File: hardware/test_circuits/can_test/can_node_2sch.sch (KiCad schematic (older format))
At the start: 32 parts, among them J201 Conn_01x05_Female, SW201 CAN1_RST, SW202 SW_SPDT, U201 MCP2562-E-P, U202 MCP2515-xSO, U203 PIC18F4620-IP, U204 L7805, Y201 40MHz, Y202 10MHz

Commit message: Realized I probably want to actually use the ~INT pin on the MCP2515 for recognizing when a transmission has successfull occured... And if I'm using that, might as well also use it for RX interrupts as well...
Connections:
- net CAN2_~INT: now reaches U202.12 (~INT)
- net CAN2_~INT: now also U203.35 (RB2/INT2/AN8)
- net CAN2_~RESET: no longer names the net of R204.2, SW201.1, U202.17 (~RESET)
- net CAN2_~RESET: no longer U203.35 (RB2/INT2/AN8)
- no-connect marks 22 -> 21
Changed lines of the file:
@@
 	1    0    0    -1
 $EndComp
-NoConn ~ 8850 2550
 Text GLabel 7650 1950 0    50   Input ~ 0
 PIC2_MOSI
@@
 Wire Wire Line
 	9300 4050 9300 4000
-Text GLabel 9500 3550 2    30   Input ~ 0
-CAN2_~RESET
-Wire Wire Line
-	9300 3550 9500 3550
+Text GLabel 8850 2550 2    30   Input ~ 0
+CAN2_~INT
 $Comp
 L power:GND #PWR0204
@@
 Connection ~ 9300 2850
 Text GLabel 4800 2300 2    30   Input ~ 0
-CAN2_~RESET
+CAN2_~INT
 Text GLabel 4800 2600 2    30   Input ~ 0
 CAN2_~RX0BF
@@
 Wire Wire Line
 	5600 1850 5600 1950
+Text GLabel 4800 4400 2    50   Input ~ 0
+PIC2_~SS
 Wire Bus Line
 	1700 3750 1700 4850
@@
 Wire Bus Line
 	5000 3150 5000 3800
-Text GLabel 4800 4400 2    50   Input ~ 0
-PIC2_~SS
 $EndSCHEMATC

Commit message: ..
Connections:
- net +5VL: now also U202.10 (~RX1BF), U202.11 (~RX0BF)
- net CAN2_~INT: now also U203.33 (RB0/INT0/FLT0/AN12); no longer U203.35 (RB2/INT2/AN8)
- removed net CAN2_~RX0BF: U202.11 (~RX0BF), U203.33 (RB0/INT0/FLT0/AN12)
- net CAN2_~RX1BF: no longer names the net of U203.34 (RB1/INT1/AN10)
- net CAN2_~RX1BF: no longer U202.10 (~RX1BF)
- no-connect marks 21 -> 23
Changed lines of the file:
@@
 Wire Wire Line
 	8850 2100 9450 2100
-Text GLabel 8850 2650 2    30   Input ~ 0
-CAN2_~RX0BF
-Text GLabel 8850 2750 2    30   Input ~ 0
-CAN2_~RX1BF
 $Comp
 L Switch:SW_Push SW201
@@
 L power:+5VL #PWR0213
 U 1 1 61B1A552
-P 9300 2850
-F 0 "#PWR0213" H 9300 2700 50  0001 C CNN
-F 1 "+5VL" H 9315 3023 50  0000 C CNN
-F 2 "" H 9300 2850 50  0001 C CNN
-F 3 "" H 9300 2850 50  0001 C CNN
-	1    9300 2850
+P 9300 2650
+F 0 "#PWR0213" H 9300 2500 50  0001 C CNN
+F 1 "+5VL" H 9450 2700 50  0000 C CNN
+F 2 "" H 9300 2650 50  0001 C CNN
+F 3 "" H 9300 2650 50  0001 C CNN
+	1    9300 2650
 	1    0    0    -1
 $EndComp
@@
 	1    0    0    -1
 $EndComp
-Connection ~ 9300 2850
-Text GLabel 4800 2300 2    30   Input ~ 0
+Text GLabel 4800 2600 2    30   Input ~ 0
 CAN2_~INT
-Text GLabel 4800 2600 2    30   Input ~ 0
-CAN2_~RX0BF
-Text GLabel 4800 2450 2    30   Input ~ 0
-CAN2_~RX1BF
 Wire Wire Line
 	5500 1850 5600 1850
@@
 Text GLabel 4800 4400 2    50   Input ~ 0
 PIC2_~SS
+NoConn ~ 4800 2450
+NoConn ~ 4800 2300
+Wire Wire Line
+	8850 2750 9300 2750
+Wire Wire Line
+	9300 2750 9300 2650
+Wire Wire Line
+	9300 2850 9300 2750
+Connection ~ 9300 2850
+Connection ~ 9300 2750
+Wire Wire Line
+	8850 2650 9300 2650
 Wire Bus Line
 	1700 3750 1700 4850
@@
 Wire Bus Line
 	5000 3150 5000 3800
+Connection ~ 9300 2650
 $EndSCHEMATC

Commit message: Complete the can_send routine --> will need to set up ISR as well still! Will include this as a comment at the end of the mcp2515.c file.
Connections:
- net +5VL: no longer U202.10 (~RX1BF), U202.11 (~RX0BF)
- no-connect marks 23 -> 25
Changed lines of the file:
@@
 L power:+5VL #PWR0213
 U 1 1 61B1A552
-P 9300 2650
-F 0 "#PWR0213" H 9300 2500 50  0001 C CNN
-F 1 "+5VL" H 9450 2700 50  0000 C CNN
-F 2 "" H 9300 2650 50  0001 C CNN
-F 3 "" H 9300 2650 50  0001 C CNN
-	1    9300 2650
+P 9300 2800
+F 0 "#PWR0213" H 9300 2650 50  0001 C CNN
+F 1 "+5VL" H 9450 2850 50  0000 C CNN
+F 2 "" H 9300 2800 50  0001 C CNN
+F 3 "" H 9300 2800 50  0001 C CNN
+	1    9300 2800
 	1    0    0    -1
 $EndComp
@@
 NoConn ~ 4800 2450
 NoConn ~ 4800 2300
+Connection ~ 9300 2850
 Wire Wire Line
-	8850 2750 9300 2750
-Wire Wire Line
-	9300 2750 9300 2650
-Wire Wire Line
-	9300 2850 9300 2750
-Connection ~ 9300 2850
-Connection ~ 9300 2750
-Wire Wire Line
-	8850 2650 9300 2650
+	9300 2800 9300 2850
+NoConn ~ 8850 2750
+NoConn ~ 8850 2650
 Wire Bus Line
 	1700 3750 1700 4850
@@
 Wire Bus Line
 	5000 3150 5000 3800
-Connection ~ 9300 2650
 $EndSCHEMATC

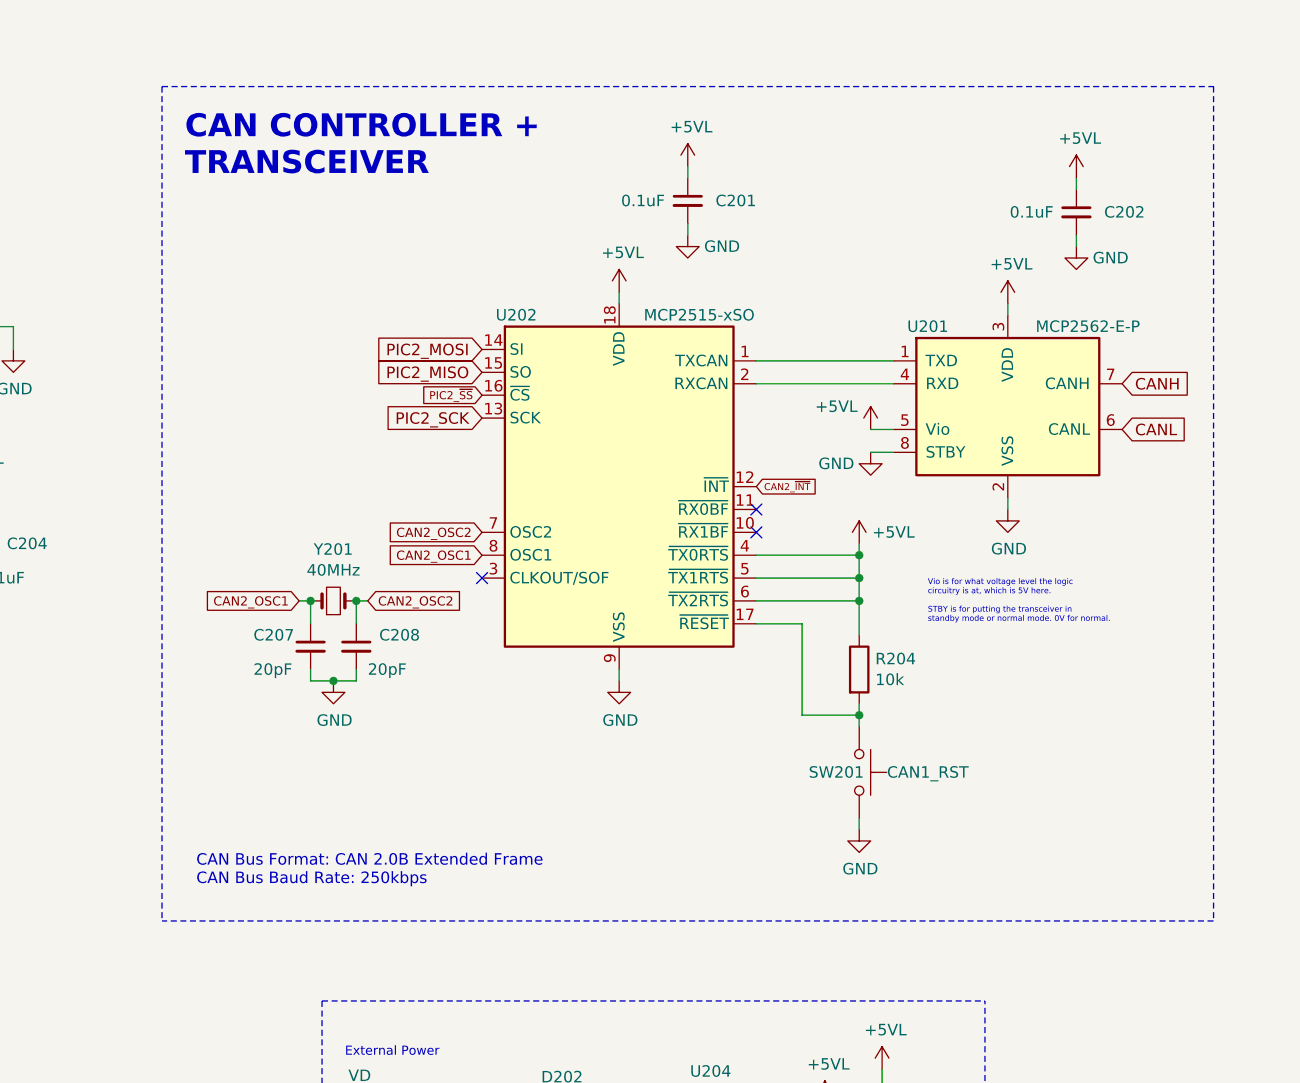
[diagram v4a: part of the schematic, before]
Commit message: Freaken forgot 120ohm termination resistors on the CANH and CANL lines! Doi!
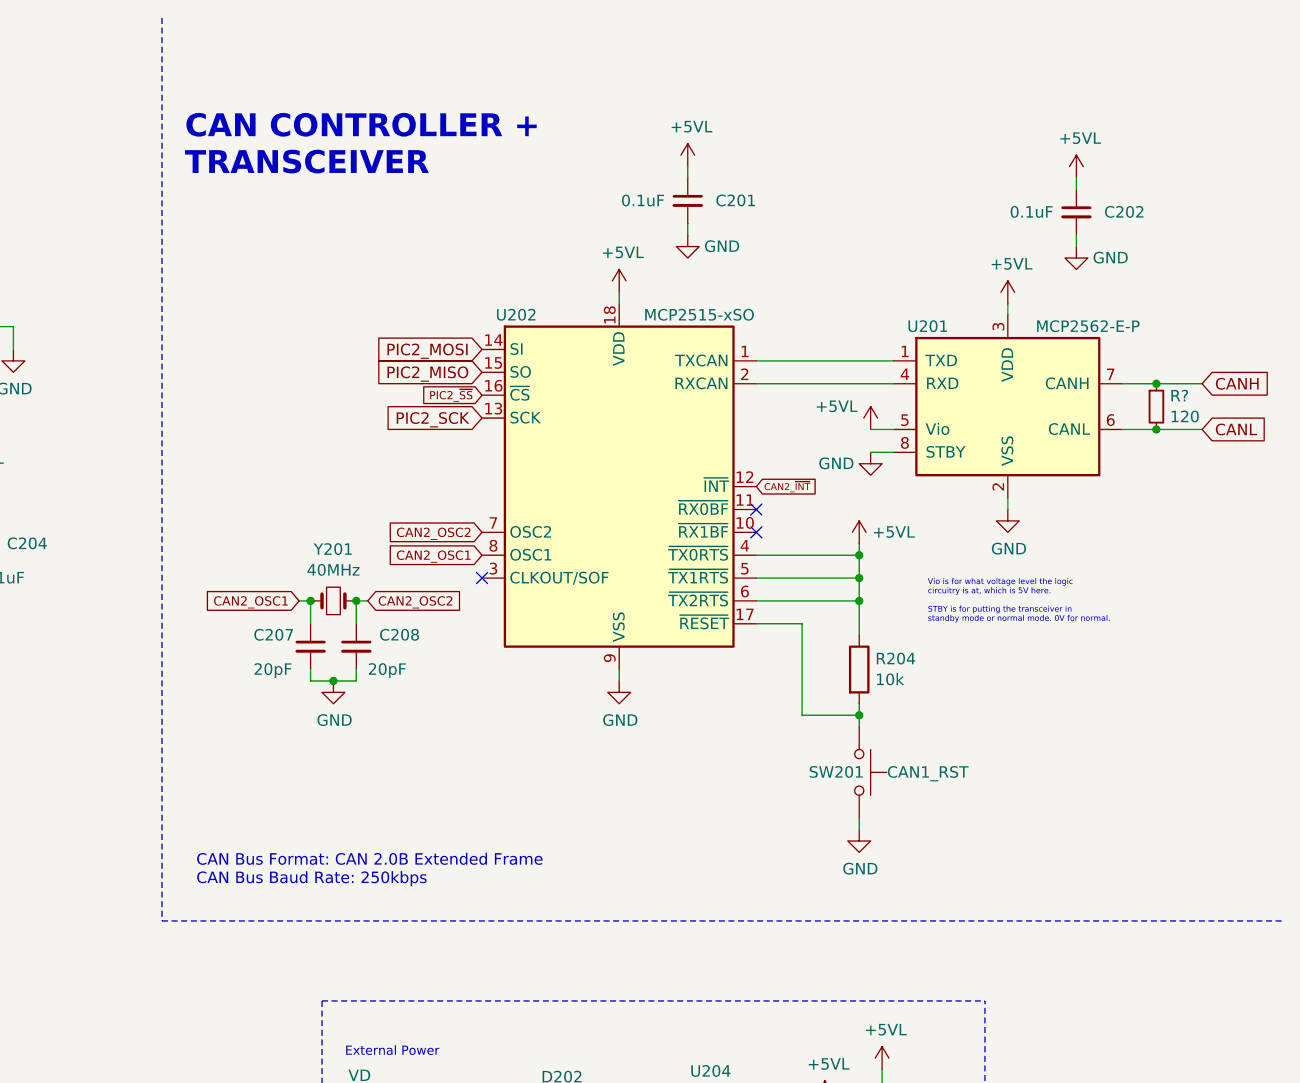
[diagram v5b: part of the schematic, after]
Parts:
- added R?: 120, symbol Device:R_Small
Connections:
- net CANH: now also R?.1
- net CANL: now also R?.2
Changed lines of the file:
@@
 Text Notes 9600 3150 0    25   ~ 0
 Vio is for what voltage level the logic\ncircuitry is at, which is 5V here.\n\nSTBY is for putting the transceiver in\nstandby mode or normal mode. 0V for normal.
-Text GLabel 10450 2100 2    50   Input ~ 0
-CANH
-Text GLabel 10450 2300 2    50   Input ~ 0
-CANL
-Wire Notes Line
-	6250 800  10850 800
-Wire Notes Line
-	10850 800  10850 4450
-Wire Notes Line
-	10850 4450 6250 4450
-Wire Notes Line
-	6250 800  6250 4450
 Text Notes 6350 1200 0    100  ~ 20
 CAN CONTROLLER +\nTRANSCEIVER
@@
 NoConn ~ 8850 2750
 NoConn ~ 8850 2650
+Text GLabel 10800 2100 2    50   Input ~ 0
+CANH
+Text GLabel 10800 2300 2    50   Input ~ 0
+CANL
+$Comp
+L Device:R_Small R?
+U 1 1 6195A1AE
+P 10600 2200
+F 0 "R?" H 10659 2246 50  0000 L CNN
+F 1 "120" H 10659 2155 50  0000 L CNN
+F 2 "" H 10600 2200 50  0001 C CNN
+F 3 "~" H 10600 2200 50  0001 C CNN
+	1    10600 2200
+	1    0    0    -1
+$EndComp
+Wire Wire Line
+	10450 2300 10600 2300
+Connection ~ 10600 2300
+Wire Wire Line
+	10600 2300 10800 2300
+Wire Wire Line
+	10800 2100 10600 2100
+Connection ~ 10600 2100
+Wire Wire Line
+	10600 2100 10450 2100
+Wire Notes Line
+	6250 500  6250 4450
+Wire Notes Line
+	6250 4450 11150 4450
 Wire Bus Line
 	1700 3750 1700 4850
